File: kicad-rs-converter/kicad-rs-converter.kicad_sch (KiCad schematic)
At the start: 0 parts

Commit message: Placed two XS's on scheme
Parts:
- added XS?: CONN_2, symbol Connector_Generic_GOST:CONN_2
- added XS?: CONN_3, symbol Connector_Generic_GOST:CONN_3
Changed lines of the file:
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@@
 	(generator_version "8.0")
 	(paper "A4")
+	(symbol
+		(lib_id "Connector_Generic_GOST:CONN_2")
+		(at 238.76 33.02 180)
+		(unit 1)
+		(exclude_from_sim no)
+		(in_bom yes)
+		(on_board yes)
+		(dnp no)
+		(property "Reference" "XS?"
+			(at 255.27 29.21 0)
+			(effects
+				(font
+					(size 2.0066 2.0066)
+				)
+				(justify right)
+			)
+		)
+		(property "Value" "CONN_2"
+			(at 238.76 22.86 0)
+			(effects
+				(font
+					(size 2.0066 2.0066)
+				)
+				(hide yes)
+			)
+		)
+		(property "Footprint" ""
+			(at 223.52 43.18 0)
+			(effects
+				(font
+					(size 2.0066 2.0066)
+				)
+				(hide yes)
+			)
+		)
+		(property "Datasheet" ""
+			(at 223.52 22.86 0)
+			(effects
+				(font
+					(size 2.0066 2.0066)
+				)
+				(hide yes)
+			)
+		)
+		(property "Description" ""
+			(at 238.76 33.02 0)
+			(effects
+				(font
+					(size 1.27 1.27)
+				)
+				(hide yes)
+			)
+		)
+		(property "PIN1" "A"
+			(at 242.062 33.02 0)
+			(effects
+				(font
+					(size 2.0066 2.0066)
+				)
+				(justify right)
+			)
+		)
+		(property "PIN2" "B"
+			(at 242.062 28.194 0)
+			(effects
+				(font
+					(size 2.0066 2.0066)
+				)
+				(justify right)
+			)
+		)
+		(pin "1"
+		)
+		(pin "2"
+		)
+		(instances
+			(project ""
+				(path "/bc93e02f-9da6-4af9-a56b-db2eb76f1927"
+					(reference "XS?")
+					(unit 1)
+				)
+			)
+		)
+	)
+	(symbol
+		(lib_id "Connector_Generic_GOST:CONN_3")
+		(at 238.76 116.84 180)
+		(unit 1)
+		(exclude_from_sim no)
+		(in_bom yes)
+		(on_board yes)
+		(dnp no)
+		(property "Reference" "XS?"
+			(at 255.27 111.125 0)
+			(effects
+				(font
+					(size 2.0066 2.0066)
+				)
+				(justify right)
+			)
+		)
+		(property "Value" "CONN_3"
+			(at 238.76 104.14 0)
+			(effects
+				(font
+					(size 2.0066 2.0066)
+				)
+				(hide yes)
+			)
+		)
+		(property "Footprint" ""
+			(at 223.52 129.54 0)
+			(effects
+				(font
+					(size 2.0066 2.0066)
+				)
+				(hide yes)
+			)
+		)
+		(property "Datasheet" ""
+			(at 223.52 104.14 0)
+			(effects
+				(font
+					(size 2.0066 2.0066)
+				)
+				(hide yes)
+			)
+		)
+		(property "Description" ""
+			(at 238.76 116.84 0)
+			(effects
+				(font
+					(size 1.27 1.27)
+				)
+				(hide yes)
+			)
+		)
+		(property "PIN1" "RX"
+			(at 239.776 119.38 0)
+			(effects
+				(font
+					(size 2.0066 2.0066)
+				)
+				(justify right)
+			)
+		)
+		(property "PIN2" "TX"
+			(at 240.03 114.3 0)
+			(effects
+				(font
+					(size 2.0066 2.0066)
+				)
+				(justify right)
+			)
+		)
+		(property "PIN3" "GND"
+			(at 238.252 109.474 0)
+			(effects
+				(font
+					(size 2.0066 2.0066)
+				)
+				(justify right)
+			)
+		)
+		(pin "2"
+		)
+		(pin "1"
+		)
+		(pin "3"
+		)
+		(instances
+			(project ""
+				(path "/bc93e02f-9da6-4af9-a56b-db2eb76f1927"
+					(reference "XS?")
+					(unit 1)
+				)
+			)
+		)
+	)
 	(sheet_instances
 		(path "/"

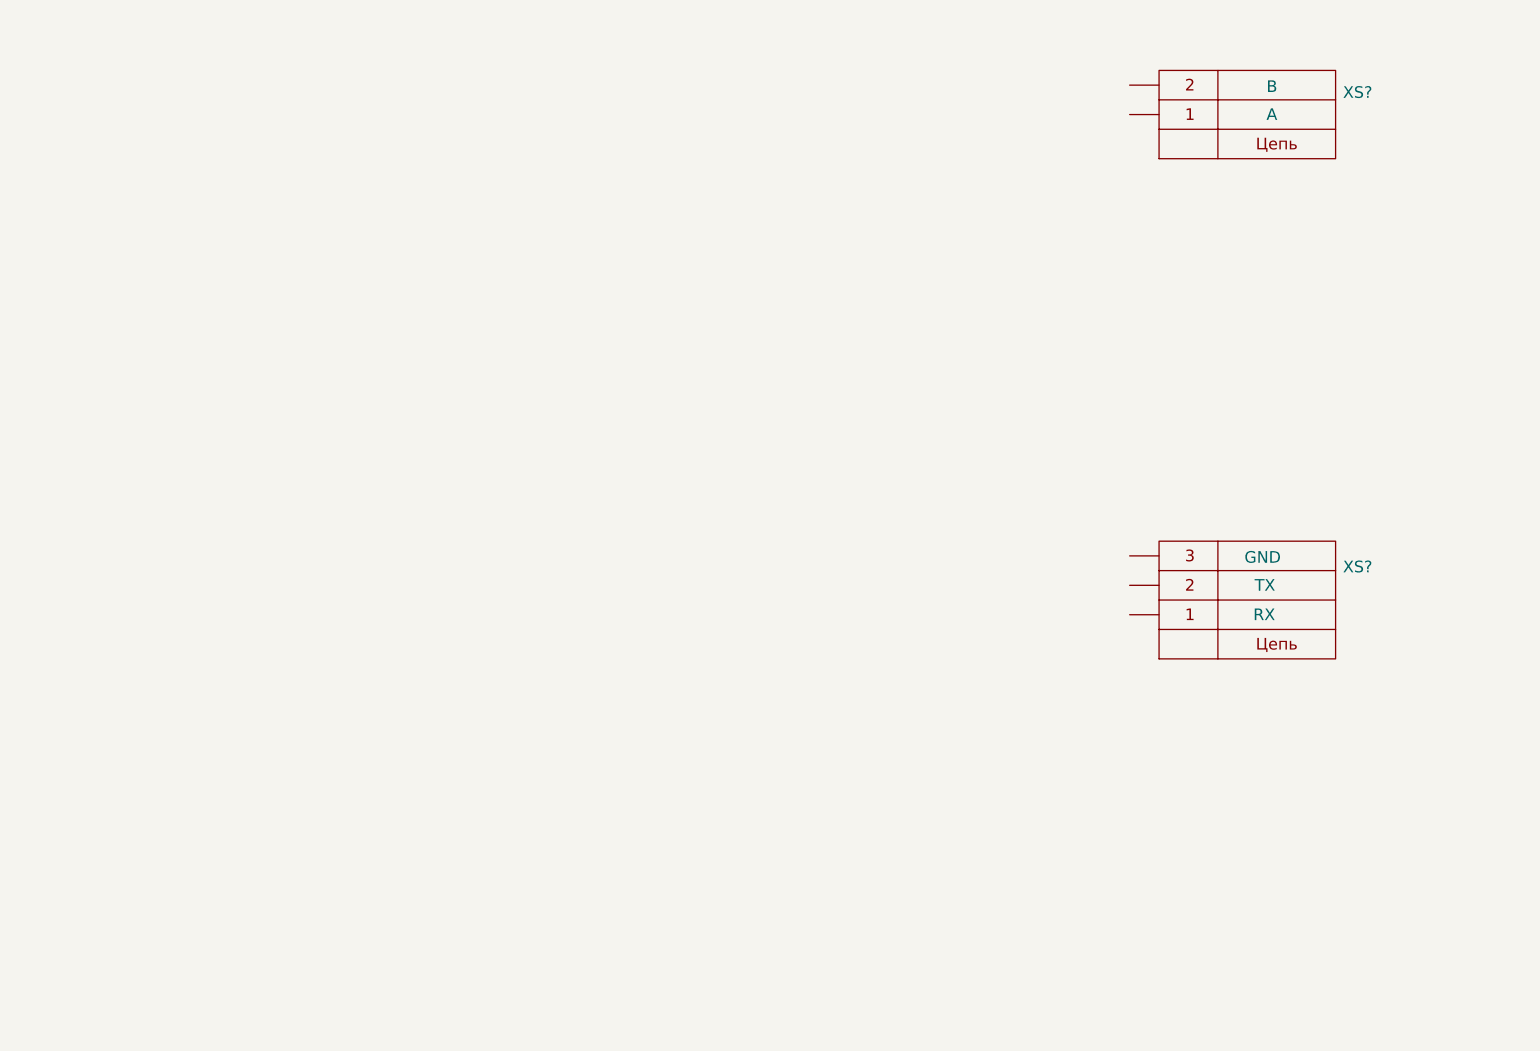
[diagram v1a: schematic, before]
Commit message: Placed MAX232 to the left as much as I could
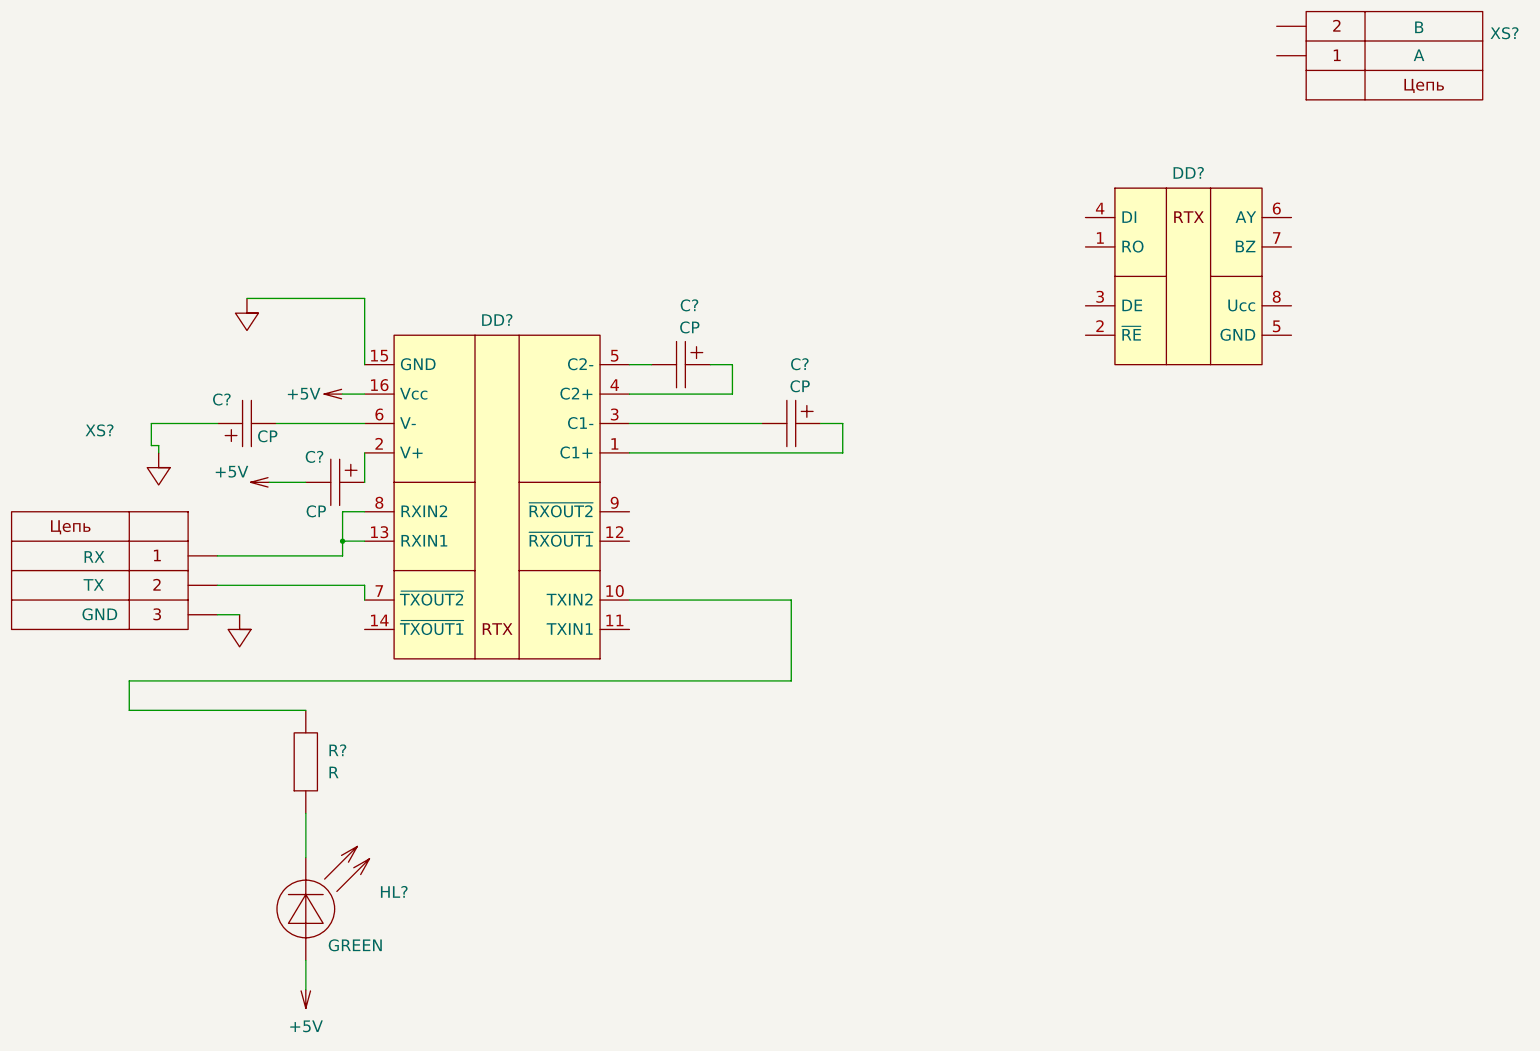
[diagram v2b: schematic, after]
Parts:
- removed XS?: CONN_3, symbol Connector_Generic_GOST:CONN_3
- added C? (x4): CP, symbol Device_GOST:CP
- added DD?: 5559ИН10У, Package_CDFP_RU:Н02.8-1В, symbol Interface_UART_GOST:5559ИН10У
- added DD?: 5559ИН1Т, Package_CDFP_RU:402.16-32, symbol Interface_UART_GOST:5559ИН1Т
- added HL?: GREEN, symbol Device_GOST:HL_LED
- added R?: R, symbol Device_GOST:R
- added XS?: CONN_3, symbol Connector_Generic_GOST:CONN_3
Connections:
- new net: C?.1, DD?.2 (V+)
- new net: C?.1, DD?.4 (C2+)
- new net: C?.2, DD?.5 (C2-)
- new net: C?.1, DD?.1 (C1+)
- new net: DD?.10 (TXIN2), R?.2
- new net: DD?.13 (RXIN1), DD?.8 (RXIN2), XS?.1
- new net: C?.2, DD?.3 (C1-)
- new net: C?.2, DD?.6 (V-)
- new net: DD?.7 (~{TXOUT2}), XS?.2
- new net: HL?.1 (K), R?.1
- new net +5V: C?.2, DD?.16 (Vcc), HL?.2 (A)
- new net GND: C?.1, DD?.15 (GND), XS?.3
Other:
- moved on the sheet: XS?

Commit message: Part of the circuit with the second LED
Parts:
- removed R?: R, symbol Device_GOST:R
- added HL?: HL_LED, symbol Device_GOST:HL_LED
- added R? (x2): R_0,25W, symbol Device_GOST:R_0,25W
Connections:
- net +5V: now also HL?.2 (A)
- net at DD?.10 (TXIN2): now also R?.2
- net at HL?.1 (K): now also R?.1
- new net: HL?.1 (K), R?.1

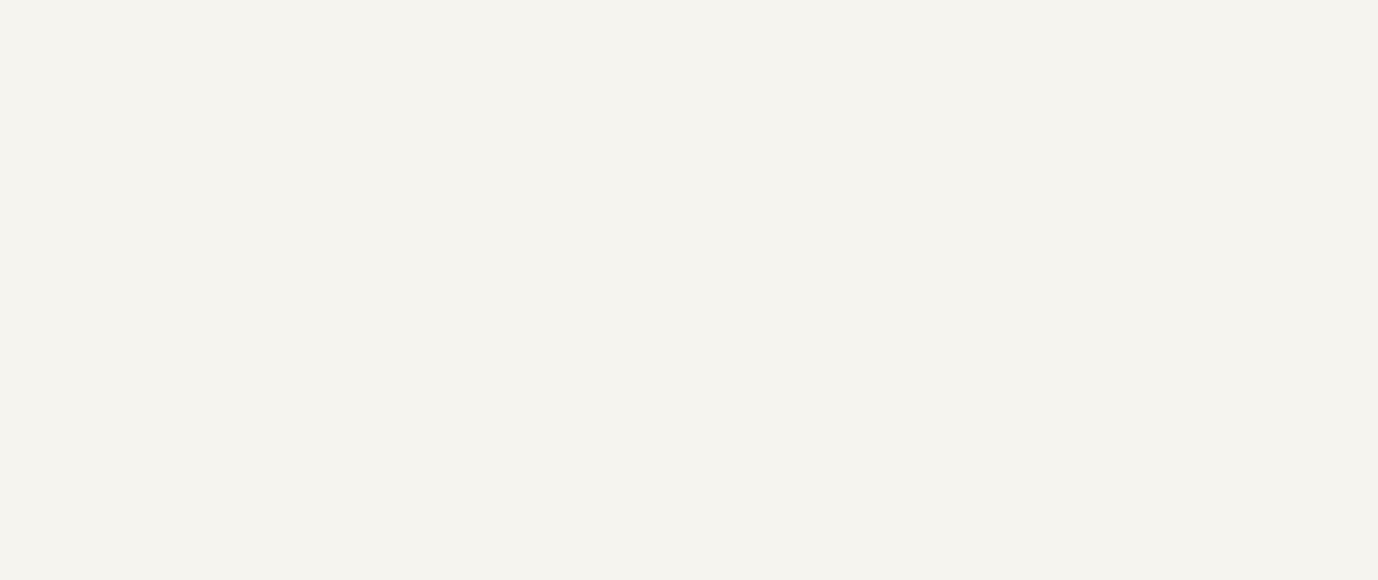
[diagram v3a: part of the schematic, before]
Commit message: Created part of circuit with voltage regulator
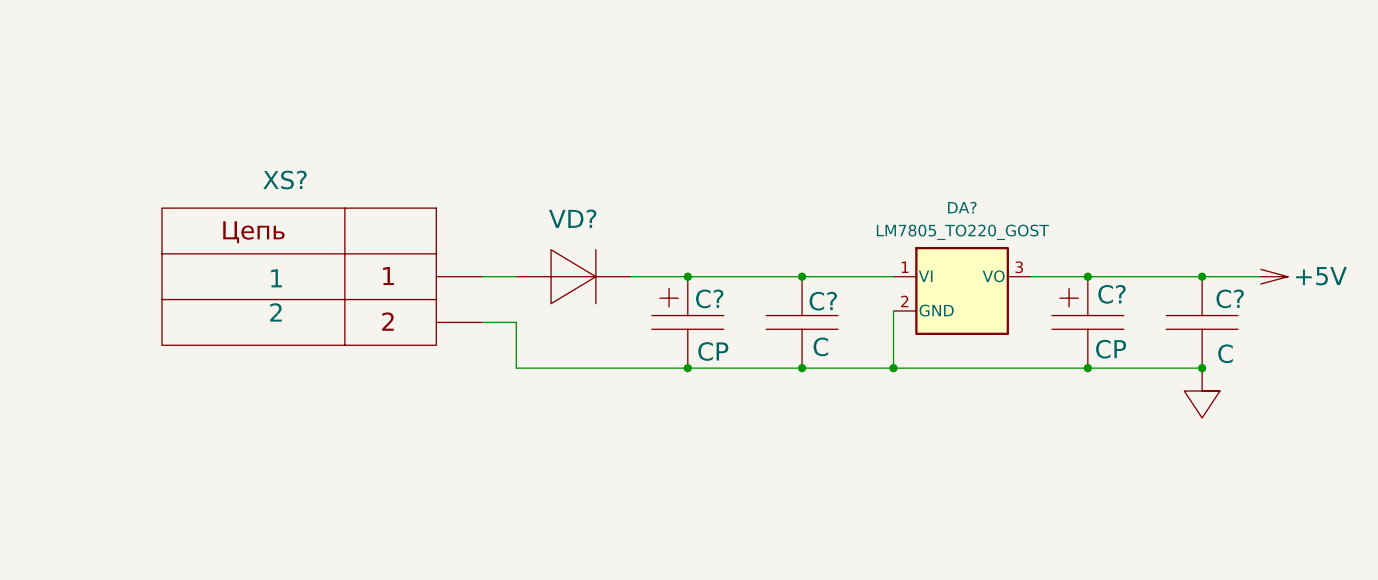
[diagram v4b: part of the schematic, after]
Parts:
- added C? (x2): CP, symbol Device_GOST:CP
- added C? (x2): C, symbol Device_GOST:C
- added DA?: LM7805_TO220_GOST, Package_TO_SOT_THT:TO-220-3_Vertical, symbol kicad-rs-converter:LM7805_TO220_GOST
- added VD?: VD, symbol Device_GOST:VD
- added XS?: CONN_2, symbol Connector_Generic_GOST:CONN_2
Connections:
- net +5V: now also C?.1, C?.1, DA?.3 (VO)
- net GND: now also C?.2, C?.2, C?.2, C?.2, DA?.2 (GND), XS?.2
- new net: C?.1, C?.1, DA?.1 (VI), VD?.1 (K)
- new net: VD?.2 (A), XS?.1

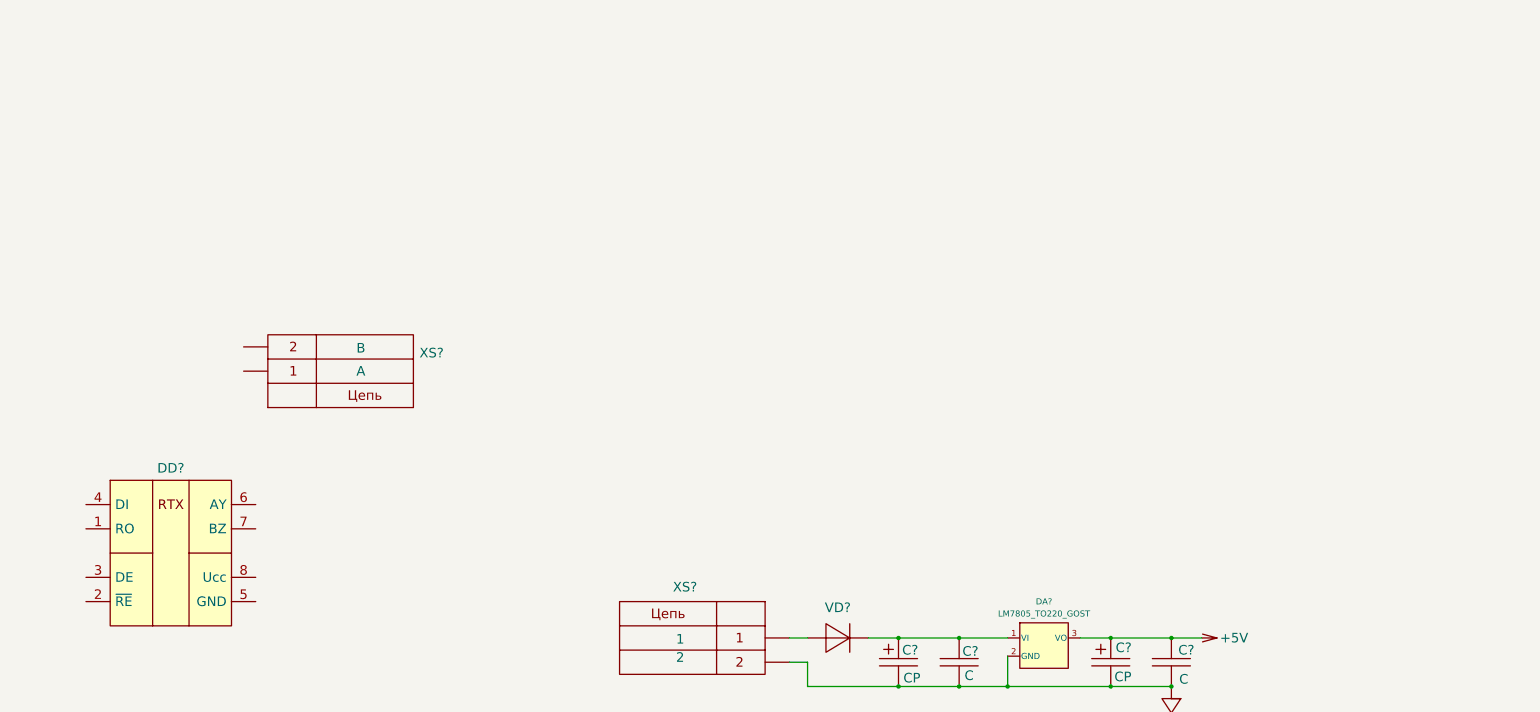
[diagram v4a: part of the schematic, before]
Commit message: Created part of circuit with MAX485 only
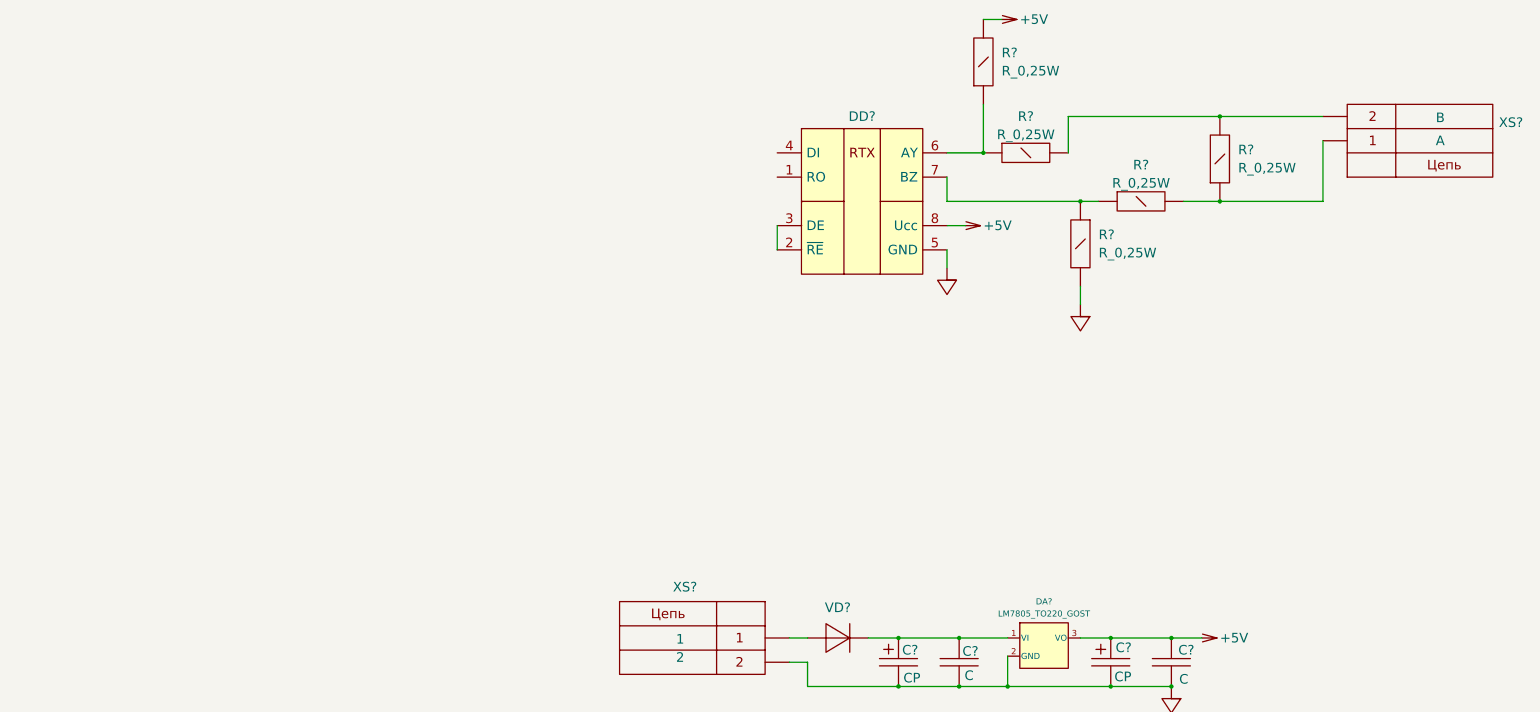
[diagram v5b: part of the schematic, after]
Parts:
- added R? (x5): R_0,25W, symbol Device_GOST:R_0,25W
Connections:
- net +5V: now also DD?.8 (Ucc), R?.2
- net GND: now also DD?.5 (GND), R?.2
- net at DD?.2 (~{RE}): now also DD?.3 (DE)
- net at DD?.6 (AY): now also R?.1, R?.1
- net at DD?.7 (BZ): now also R?.1, R?.1
- net at XS?.1: now also R?.1, R?.2
- net at XS?.2: now also R?.2, R?.2
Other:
- moved on the sheet: DD?, XS?
